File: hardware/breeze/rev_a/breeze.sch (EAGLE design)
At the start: 11 parts, among them J3 IMPULSE_GECKO_HEADER, U1 RV-3049-C3, U2 FM25V20-DG

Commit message: some parts on breeze
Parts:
- removed BT1: ML-1220/F1AN, batteries:ML-1220/F1AN
- removed C1: 10nF, passives:CAPACITOR
- removed C2: 0.1uF, passives:CAPACITOR
- removed R1, R2: 4.7k, passives:RESISTOR
- removed R3, R4: 10k, passives:RESISTOR
- removed U1: RV-3049-C3, chips:RV-3049-C3
- removed U2: FM25V20-DG, chips:FM25V20-DG
- added Q1: NX3008PBK, fets:NX3008PBK
- added R6: 100k, rcl:R-US_R0603
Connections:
- removed net !FRAM_CS: J3.TRIGGER/P2.1, R1.1, U2.!CS
- removed net BATTERY: BT1.+, C1.1, U1.VCC
- removed net N$6: R4.2, U1.VBACKUP
- removed net N$7: R3.2, U1.CLKOE
- removed net RTC_CS: J3.OVRVLT/P1.7, R2.2, U1.!CS
- new net AIRFLOW_CTRL: J3.OVRVLT/P1.7, Q1.G, R6.1
- new net AIRFLOW_VCC: Q1.S
- new net TRIGGER: J3.TRIGGER/P2.1
- net GND: no longer BT1.-, C1.2, C2.2, R2.1, R3.1, R4.1, U1.GND, U2.VSS
- net MISO0: no longer U1.MISO, U2.SO
- net MOSI0: no longer U1.MOSI, U2.SI
- net SCLK0: no longer U1.SCL, U2.SCK
- net VCC: now also Q1.D, R6.2; no longer C2.1, R1.2, U2.!HOLD, U2.!WP, U2.VDD
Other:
- note removed: "FRAM"

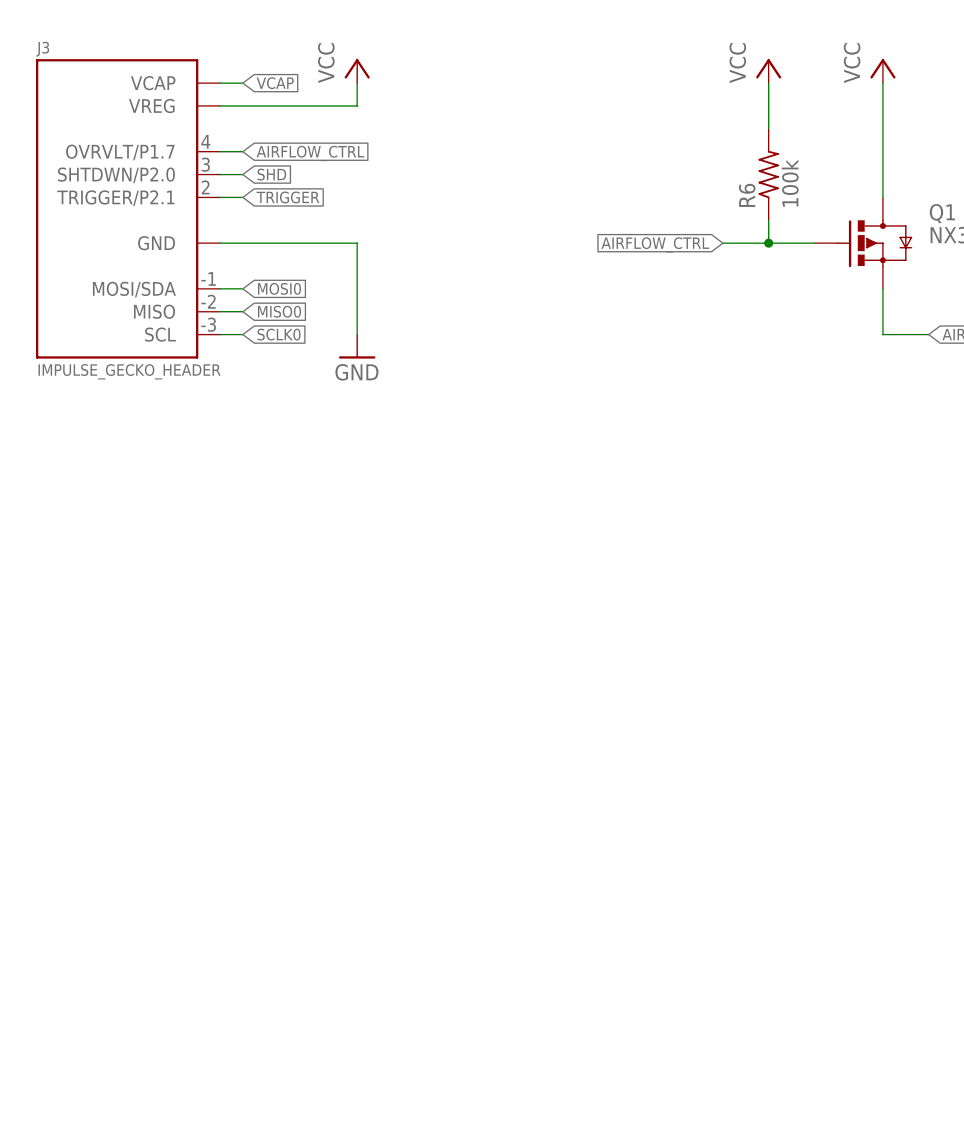
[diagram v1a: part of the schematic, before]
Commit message: simple breeze board routed
needs another pass when i get parts
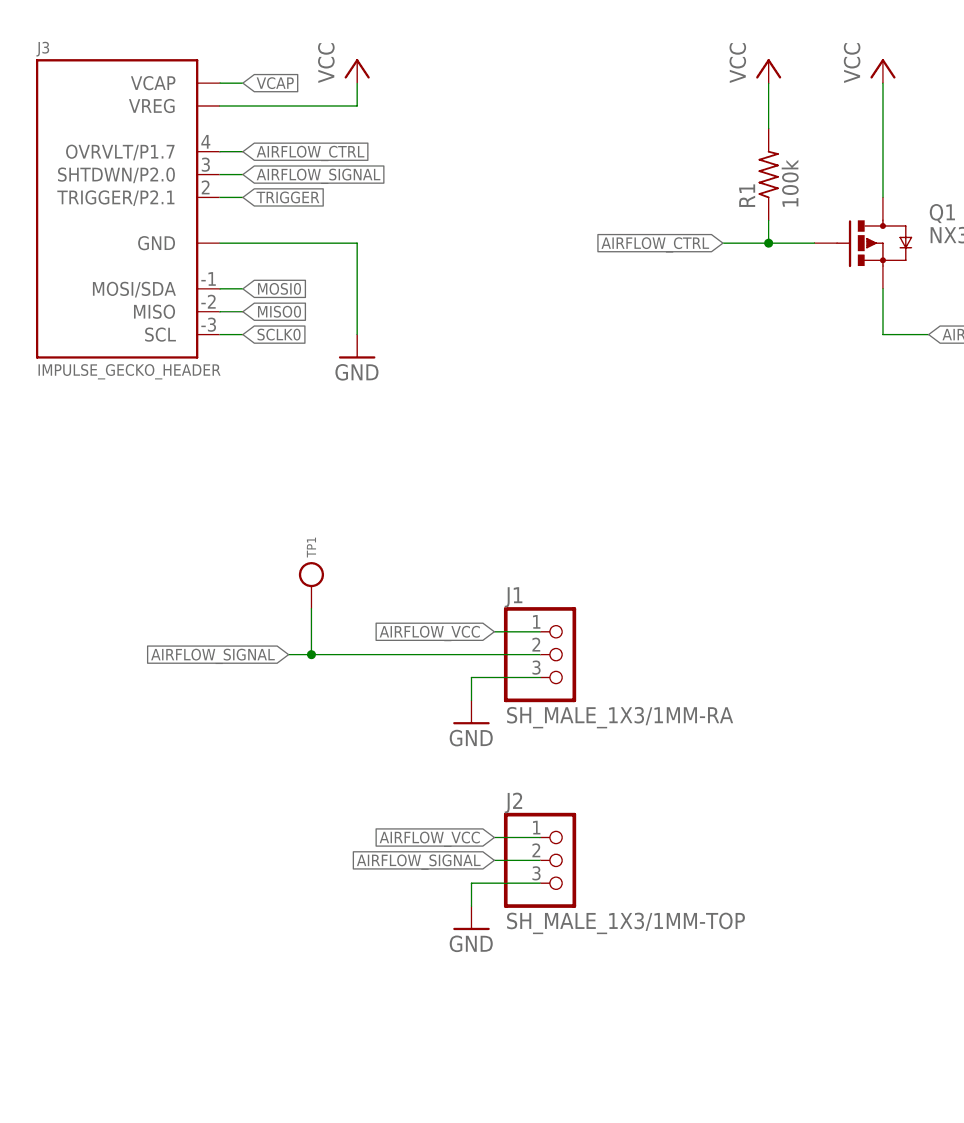
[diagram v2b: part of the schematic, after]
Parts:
- added J1: SH_MALE_1X3/1MM-RA, headers:SH_MALE_1X3/1MM-RA
- added J2: SH_MALE_1X3/1MM-TOP, headers:SH_MALE_1X3/1MM-TOP
- added TP1: TEST_POINT_0.040IN, headers:TEST_POINT_0.040IN
- renumbered R6 to R1
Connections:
- removed net SHD: J3.SHTDWN/P2.0
- new net AIRFLOW_SIGNAL: J1.2, J2.2, J3.SHTDWN/P2.0, TP1.TESTPOINT
- net AIRFLOW_VCC: now also J1.1, J2.1
- net GND: now also J1.3, J2.3
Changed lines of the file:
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@@
 <part name="LOGO1" library="logos" deviceset="UMICH_SOLID" device="_TINY"/>
 <part name="Q1" library="fets" deviceset="NX3008PBK" device=""/>
-<part name="R6" library="rcl" deviceset="R-US_" device="R0603" value="100k"/>
+<part name="R1" library="rcl" deviceset="R-US_" device="R0603" value="100k"/>
 <part name="P+3" library="supply1" deviceset="VCC" device=""/>
 <part name="P+4" library="supply1" deviceset="VCC" device=""/>
+<part name="J1" library="headers" deviceset="SH_MALE_1X3/1MM" device="-RA"/>
+<part name="J2" library="headers" deviceset="SH_MALE_1X3/1MM" device="-TOP"/>
+<part name="GND2" library="supply1" deviceset="GND" device=""/>
+<part name="GND3" library="supply1" deviceset="GND" device=""/>
+<part name="TP1" library="headers" deviceset="TEST_POINT_0.040IN" device=""/>
 </parts>
 <sheets>
@@
 <instance part="LOGO1" gate="G$1" x="233.172" y="173.99"/>
 <instance part="Q1" gate="G$1" x="111.76" y="137.16"/>
-<instance part="R6" gate="G$1" x="99.06" y="144.78" rot="R90"/>
+<instance part="R1" gate="G$1" x="99.06" y="144.78" rot="R90"/>
 <instance part="P+3" gate="VCC" x="99.06" y="157.48"/>
 <instance part="P+4" gate="VCC" x="111.76" y="157.48"/>
+<instance part="J1" gate="G$1" x="76.2" y="91.44"/>
+<instance part="J2" gate="G$1" x="76.2" y="68.58"/>
+<instance part="GND2" gate="1" x="66.04" y="83.82"/>
+<instance part="GND3" gate="1" x="66.04" y="60.96"/>
+<instance part="TP1" gate="G$1" x="48.26" y="99.06" rot="R270"/>
 </instances>
 <busses>
@@
 <pinref part="J3" gate="G$1" pin="GND"/>
 </segment>
+<segment>
+<pinref part="J1" gate="G$1" pin="3"/>
+<wire x1="73.66" y1="88.9" x2="66.04" y2="88.9" width="0.1524" layer="91"/>
+<wire x1="66.04" y1="88.9" x2="66.04" y2="86.36" width="0.1524" layer="91"/>
+<pinref part="GND2" gate="1" pin="GND"/>
+</segment>
+<segment>
+<pinref part="J2" gate="G$1" pin="3"/>
+<wire x1="73.66" y1="66.04" x2="66.04" y2="66.04" width="0.1524" layer="91"/>
+<wire x1="66.04" y1="66.04" x2="66.04" y2="63.5" width="0.1524" layer="91"/>
+<pinref part="GND3" gate="1" pin="GND"/>
+</segment>
 </net>
 <net name="VCC" class="0">
@@
 </segment>
 <segment>
-<pinref part="R6" gate="G$1" pin="2"/>
+<pinref part="R1" gate="G$1" pin="2"/>
 <wire x1="99.06" y1="149.86" x2="99.06" y2="154.94" width="0.1524" layer="91"/>
 <pinref part="P+3" gate="VCC" pin="VCC"/>
@@
 <pinref part="J3" gate="G$1" pin="VCAP"/>
 <wire x1="40.64" y1="154.94" x2="38.1" y2="154.94" width="0.1524" layer="91"/>
-</segment>
-</net>
-<net name="SHD" class="0">
-<segment>
-<label x="40.64" y="144.78" size="1.27" layer="95" xref="yes"/>
-<pinref part="J3" gate="G$1" pin="SHTDWN/P2.0"/>
-<wire x1="40.64" y1="144.78" x2="38.1" y2="144.78" width="0.1524" layer="91"/>
 </segment>
 </net>
@@
 <label x="116.84" y="127" size="1.27" layer="95" xref="yes"/>
 </segment>
+<segment>
+<pinref part="J1" gate="G$1" pin="1"/>
+<wire x1="73.66" y1="93.98" x2="68.58" y2="93.98" width="0.1524" layer="91"/>
+<label x="68.58" y="93.98" size="1.27" layer="95" rot="R180" xref="yes"/>
+</segment>
+<segment>
+<pinref part="J2" gate="G$1" pin="1"/>
+<wire x1="73.66" y1="71.12" x2="68.58" y2="71.12" width="0.1524" layer="91"/>
+<label x="68.58" y="71.12" size="1.27" layer="95" rot="R180" xref="yes"/>
+</segment>
 </net>
 <net name="AIRFLOW_CTRL" class="0">
@@
 </segment>
 <segment>
-<pinref part="R6" gate="G$1" pin="1"/>
+<pinref part="R1" gate="G$1" pin="1"/>
 <wire x1="99.06" y1="139.7" x2="99.06" y2="137.16" width="0.1524" layer="91"/>
 <pinref part="Q1" gate="G$1" pin="G"/>
@@
 </segment>
 </net>
+<net name="AIRFLOW_SIGNAL" class="0">
+<segment>
+<pinref part="J1" gate="G$1" pin="2"/>
+<wire x1="73.66" y1="91.44" x2="48.26" y2="91.44" width="0.1524" layer="91"/>
+<label x="45.72" y="91.44" size="1.27" layer="95" rot="R180" xref="yes"/>
+<pinref part="TP1" gate="G$1" pin="TESTPOINT"/>
+<wire x1="48.26" y1="91.44" x2="45.72" y2="91.44" width="0.1524" layer="91"/>
+<wire x1="48.26" y1="96.52" x2="48.26" y2="91.44" width="0.1524" layer="91"/>
+<junction x="48.26" y="91.44"/>
+</segment>
+<segment>
+<pinref part="J2" gate="G$1" pin="2"/>
+<wire x1="73.66" y1="68.58" x2="68.58" y2="68.58" width="0.1524" layer="91"/>
+<label x="68.58" y="68.58" size="1.27" layer="95" rot="R180" xref="yes"/>
+</segment>
+<segment>
+<label x="40.64" y="144.78" size="1.27" layer="95" xref="yes"/>
+<pinref part="J3" gate="G$1" pin="SHTDWN/P2.0"/>
+<wire x1="40.64" y1="144.78" x2="38.1" y2="144.78" width="0.1524" layer="91"/>
+</segment>
+</net>
